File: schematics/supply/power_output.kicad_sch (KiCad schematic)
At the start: 41 parts, among them Q10 IRLML0030, Q6 STP13NK60Z, Q7 STP13NK60Z, U18 TL331, U19 INA169, U5 EL817, U9 IRS2153S

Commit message: Found and fixed issues in schematics.
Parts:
- R31, R32: value 5 -> 10
- R39: value 1K -> 680
- R39: value 70K -> 68K
- R39: value 30K -> 33K
- TR2: value ETD 49/25/16@N87 N19@1mm*2/7+7@1mm*4 -> ETD 49/25/16@N87 N18@1mm*2/7+7@1mm*4
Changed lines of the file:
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@@
     (stroke (width 0) (type default))
+  )
+  (text_box "Known issues:\n- Power Output generation will starts up when +5VSYS line is OFF"
+    (at 198.12 195.58 0) (size 82.55 76.2)
+    (stroke (width 0) (type default))
+    (fill (type none))
+    (effects (font (size 1.27 1.27)) (justify left top))
   )
   (text "100 KHz" (at 137.16 144.78 0)
@@
   (symbol (lib_id "Device:R") (at 176.53 114.3 90) (unit 1)
     (in_bom yes) (on_board yes) (dnp no) (fields_autoplaced)
-    (property "Reference" "R31" (at 176.53 109.22 90)
-      (effects (font (size 1.27 1.27)))
-    )
-    (property "Value" "5" (at 176.53 111.76 90)
+    (property "Reference" "R31" (at 176.53 107.95 90)
+      (effects (font (size 1.27 1.27)))
+    )
+    (property "Value" "10" (at 176.53 110.49 90)
       (effects (font (size 1.27 1.27)))
     )
@@
       (effects (font (size 1.27 1.27)))
     )
-    (property "Value" "1K" (at 337.82 95.25 0)
+    (property "Value" "680" (at 337.82 95.25 0)
       (effects (font (size 1.27 1.27)))
     )
@@
   (symbol (lib_id "Device:R") (at 176.53 146.05 90) (unit 1)
     (in_bom yes) (on_board yes) (dnp no) (fields_autoplaced)
-    (property "Reference" "R32" (at 176.53 140.97 90)
-      (effects (font (size 1.27 1.27)))
-    )
-    (property "Value" "5" (at 176.53 143.51 90)
+    (property "Reference" "R32" (at 176.53 139.7 90)
+      (effects (font (size 1.27 1.27)))
+    )
+    (property "Value" "10" (at 176.53 142.24 90)
       (effects (font (size 1.27 1.27)))
     )
@@
       (effects (font (size 1.27 1.27)))
     )
-    (property "Value" "70K" (at 292.1 91.44 90)
+    (property "Value" "68K" (at 292.1 91.44 90)
       (effects (font (size 1.27 1.27)))
     )
@@
       (effects (font (size 1.27 1.27)))
     )
-    (property "Value" "30K" (at 295.91 101.6 0)
+    (property "Value" "33K" (at 295.91 101.6 0)
       (effects (font (size 1.27 1.27)))
     )
@@
       (effects (font (size 1.27 1.27)))
     )
-    (property "Value" "ETD 49/25/16@N87 N19@1mm*2/7+7@1mm*4" (at 226.06 119.38 0)
-      (effects (font (size 1.27 1.27)))
-    )
+    (property "Value" "ETD 49/25/16@N87 N18@1mm*2/7+7@1mm*4" (at 226.06 119.38 0)
+      (effects (font (size 1.27 1.27)))
+    )

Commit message: Some changes
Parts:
- C17: value 100 nF -> 1 uF
- R53: value 49K5 -> 47K
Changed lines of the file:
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@@
       (effects (font (size 1.27 1.27)) (justify right))
     )
-    (property "Value" "49K5" (at 360.68 168.91 0)
+    (property "Value" "47K" (at 360.68 168.91 0)
       (effects (font (size 1.27 1.27)) (justify right))
     )
@@
       (effects (font (size 1.27 1.27)) (justify right))
     )
-    (property "Value" "100 nF" (at 121.92 114.3 0)
-      (effects (font (size 1.27 1.27)) (justify right))
-    )
+    (property "Value" "1 uF" (at 121.92 114.3 0)
+      (effects (font (size 1.27 1.27)) (justify right))
+    )

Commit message: Continue soldering and setting up hardware
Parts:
- D16: value SS16 -> STTH1R06A
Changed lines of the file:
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@@
   (symbol (lib_id "Device:D") (at 162.56 114.3 180) (unit 1)
     (in_bom yes) (on_board yes) (dnp no) (fields_autoplaced)
-    (property "Reference" "D16" (at 162.56 109.22 0)
+    (property "Reference" "D16" (at 162.56 107.95 0)
       (effects (font (size 1.27 1.27)))
     )
-    (property "Value" "SS16" (at 162.56 111.76 0)
+    (property "Value" "STTH1R06A" (at 162.56 110.49 0)
       (effects (font (size 1.27 1.27)))
     )

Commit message: supply board - power controllers changed; PWM logic changed
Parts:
- removed C17, C18, C21: 1 uF, Capacitor_SMD:C_0603_1608Metric, symbol Device:C
- removed C18: 22 uF, Capacitor_SMD:C_1210_3225Metric, symbol Device:C
- removed C19: 470 pF, Capacitor_SMD:C_0603_1608Metric, symbol Device:C
- removed D22: GNL-3012GD, Connector_JST:JST_XH_B2B-XH-A_1x02_P2.50mm_Vertical, symbol Device:LED
- removed Q10: IRLML0030, Package_TO_SOT_SMD:SOT-23, symbol Transistor_FET:IRLML0030
- removed Q6, Q7: STP13NK60Z, Package_TO_SOT_THT:TO-220-3_Vertical, symbol Device:Q_NMOS_GDS
- removed R25: 510, Resistor_SMD:R_0805_2012Metric, symbol Device:R
- removed R27: 10K, Resistor_SMD:R_0805_2012Metric, symbol Device:R
- removed R31, R32: 10, Resistor_SMD:R_0805_2012Metric, symbol Device:R
- removed R39: 680, Resistor_SMD:R_0805_2012Metric, symbol Device:R
- removed R39: 68K, Resistor_SMD:R_0805_2012Metric, symbol Device:R
- removed R39: 33K, Resistor_SMD:R_0805_2012Metric, symbol Device:R
- removed TP2: POWER_OUTPUT, TestPoint:TestPoint_Pad_D2.0mm, symbol Connector:TestPoint
- removed U18: TL331, Package_TO_SOT_SMD:SOT-23-5, symbol Comparator:TL331
- removed U5: EL817, Package_DIP:DIP-4_W7.62mm, symbol Isolator:EL817
- removed U9: IRS2153S, Package_SO:SOP-8_3.76x4.96mm_P1.27mm, symbol Driver_FET:IR2153
- added C10: 2 nF, Capacitor_SMD:C_0603_1608Metric, symbol Device:C
- added C16: 2200 uF@63V, Capacitor_THT:CP_Radial_D18.0mm_P7.50mm, symbol Device:C_Polarized
- added C4, C54: 1 uF, Capacitor_SMD:C_0603_1608Metric, symbol Device:C
- added C55, C67: 100 nF, Capacitor_SMD:C_0603_1608Metric, symbol Device:C
- added Q2, Q3: STP13NK60Z, Package_TO_SOT_THT:TO-220-3_Vertical, symbol Device:Q_NMOS_GDS
- added Q7 (x3): IRLML0030, Package_TO_SOT_SMD:SOT-23, symbol Transistor_FET:IRLML0030
- added R1 (x2): 220, Resistor_SMD:R_0805_2012Metric, symbol Device:R
- added R47: 22, Resistor_SMD:R_0805_2012Metric, symbol Device:R
- added R54, R56, R64, R68 (x2): 10K, Resistor_SMD:R_0805_2012Metric, symbol Device:R
- added R68: 1K, Resistor_SMD:R_0805_2012Metric, symbol Device:R
- added R9: 5K, Resistor_SMD:R_0805_2012Metric, symbol Device:R
- added U2 (x2): EL817, Package_DIP:DIP-4_W7.62mm, symbol Isolator:EL817
- added U23 (x2): IR2117, Package_SO:SOIC-8_3.9x4.9mm_P1.27mm, symbol My_Library:IR2117
- added U30: UC3525, Package_SO:SOIC-16W_7.5x10.3mm_P1.27mm, symbol Regulator_Controller:UC3525
- C14, C16: value CK45-B3DD331KYGNA -> К73-17 0.33 uF@630V; footprint Capacitor_THT:C_Disc_D7.5mm_W5.0mm_P5.00mm -> Capacitor_THT:C_Rect_L24.0mm_W12.2mm_P22.50mm_MKT
- R25: value 5K1@2W -> 100@2W
- renumbered R49 to R56, R50 to R57, R52 to R58, R53 to R59, U19 to U27
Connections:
- net +5V_VSYS: now also R1.2, R1.2
- net 400V: now also Q2.2 (D)
- net GND: now also C16.2, Q7.2 (S), Q7.2 (S), R68.1
- net GNDPWR: now also C10.2, C4.1, C55.2, C67.2, Q3.3 (S), Q7.2 (S), R56.2, R64.2, R68.2, R9.2, U23.3 (GND), U23.3 (GND), U23.6 (VS), U30.12 (GND)
- net POWER_OUTPUT_FB: now also Q7.1 (G)
- net RC_SNABBER_MIDDLEPOINT: now also C54.2, Q2.3 (S), Q3.2 (D), U23.6 (VS)
- net V_STANDBY: now also C4.2, U23.1 (VCC), U23.1 (VCC), U23.8 (VB), U30.13 (VC), U30.15 (VIN)
- net at D16.1 (K): now also C54.1, U23.8 (VB)
- net at D23.2 (K), L3.1: now also C16.1
- new net: R1.1, U2.1 (x2)
- new net: Q3.1 (G), U23.7 (OUT)
- new net: Q7.3 (D), U2.2 (x2)
- new net: Q7.1 (G), R68.1, U2.3
- new net: R9.1, U30.6 (RT)
- new net: U23.2 (IN), U30.11 (OUTA)
- new net: Q2.1 (G), U23.7 (OUT)
- new net: U23.2 (IN), U30.14 (OUTB)
- new net: C10.1, R47.1, U30.5 (CT)
- new net: R47.2, U30.7 (DISCH)
- new net: C55.1, U30.8 (SS)
- new net DCDC_2V5_VREF: R54.2, R56.1, U30.2 (NI)
- new net DCDC_5V_VREF: C67.1, R54.1, R68.1, U2.4, U2.4, U30.16 (REF)
- new net DCDC_FEEDBACK: R64.1, U2.3, U30.1 (INV)
- new net DCDC_SHUTDOWN: Q7.3 (D), R68.2, U30.10 (SD)
- new net PWR_SHUTDOWN#: Q7.1 (G), R68.2
- no-connect marks 0 -> 3
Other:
- note removed: "100 KHz"
- moved on the sheet: C14, C16, C18, C23, C24, CLR2, CLR3, CLR4, D23, L3, R25, R56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

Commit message: re-design supply board
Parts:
- added TP2: PW_B, TestPoint:TestPoint_Pad_1.0x1.0mm, symbol Connector:TestPoint
- added TP2: PW_A, TestPoint:TestPoint_Pad_1.0x1.0mm, symbol Connector:TestPoint
- renumbered R56 to R59, R57 to R60, R58 to R61, R59 to R62
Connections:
- net at U23.2 (IN), U30.11 (OUTA): now also TP2.1
- net at U23.2 (IN), U30.14 (OUTB): now also TP2.1

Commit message: Continue project
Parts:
- C51: renamed from C10; value 2 nF -> 2.2 nF
- C53: renamed from C4; value 1 uF -> 10 uF
- R50: renamed from R9; value 5K -> 2K2
- renumbered C67 to C50, C55 to C52, C23 to C55, C14 to C56, C24 to C57, C16 to C58, C16 to C59, C16 to C60, C18 to C61, C18 to C62, C18 to C63, D16 to D21, D23 to D22, L3 to L4, Q2 to Q10, Q3 to Q11, Q7 to Q8, Q7 to Q9, R54 to R48, R56 to R49, R68 to R51, R47 to R52, R1 to R53, R1 to R54, R64 to R55, R68 to R56, R68 to R57, R25 to R58, TP2 to TP17, TP2 to TP18, U2 to U22, U2 to U23, U30 to U24, U23 to U25, U23 to U26
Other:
- moved on the sheet: R50

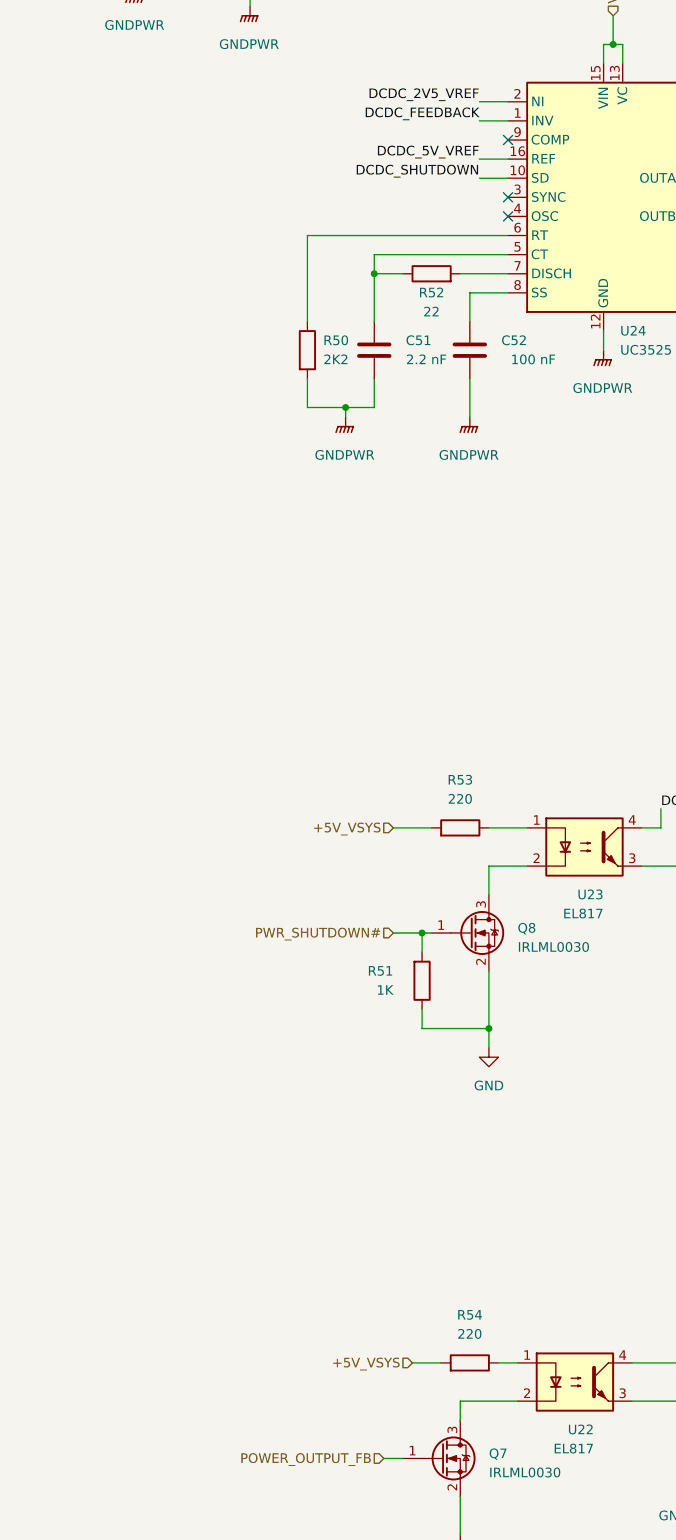
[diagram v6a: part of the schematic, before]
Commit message: some changes in schema. I found additional error. This commit saves changes before re-write some blocks
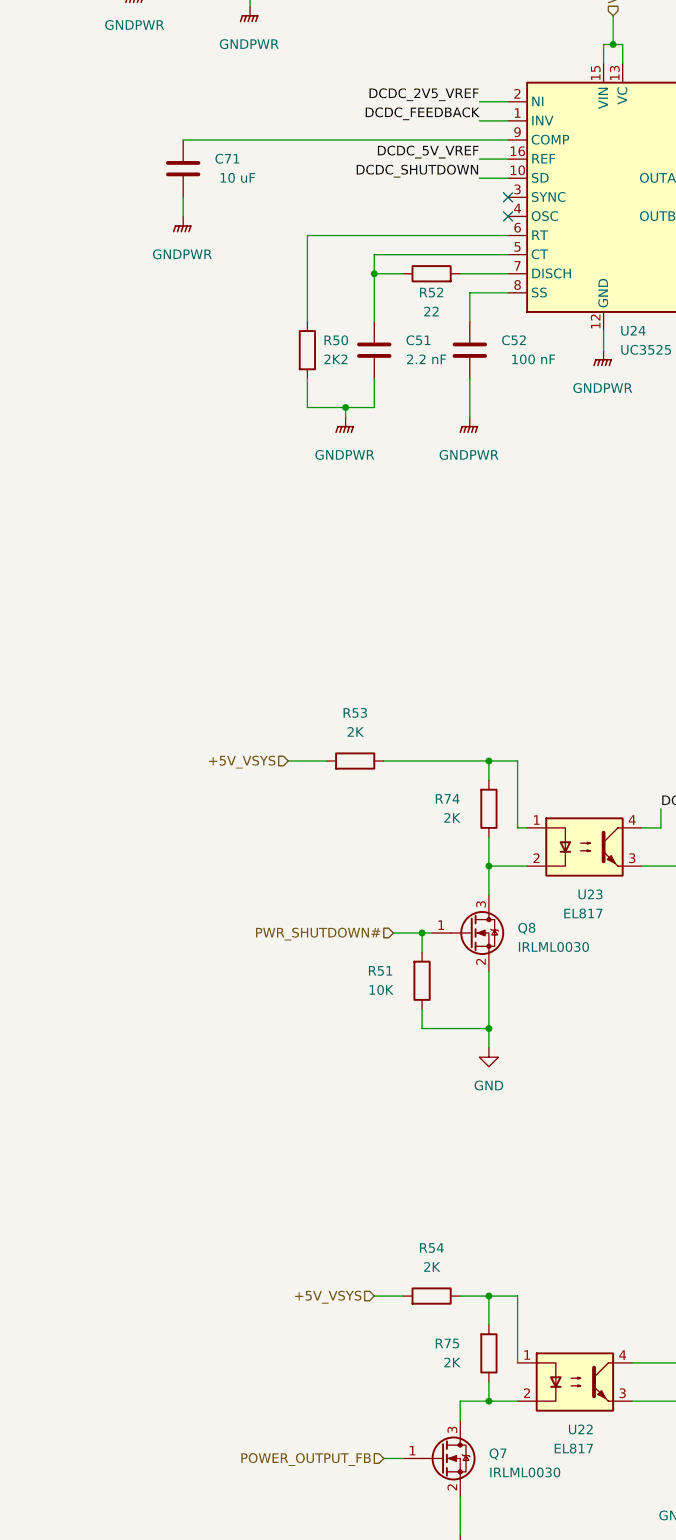
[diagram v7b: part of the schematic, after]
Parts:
- added C71: 10 uF, Capacitor_SMD:C_0603_1608Metric, symbol Device:C
- added R74, R75: 2K, Resistor_SMD:R_0805_2012Metric, symbol Device:R
- R51: value 1K -> 10K
- R53, R54: value 220 -> 2K
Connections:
- net GNDPWR: now also C71.2
- net at R54.1, U22.1: now also R75.2
- net at Q7.3 (D), U22.2: now also R75.1
- net at U24.9 (COMP): now also C71.1
- net at R53.1, U23.1: now also R74.2
- net at Q8.3 (D), U23.2: now also R74.1
- no-connect marks 3 -> 2
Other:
- moved on the sheet: R53, R54

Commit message: debugging DCDC converters... Standby supply works fine (noise level = 1,7%). At now Starting to debug PFC module
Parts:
- removed C54: 1 uF, Capacitor_SMD:C_0603_1608Metric, symbol Device:C
- removed C56, C58: К73-17 0.33 uF@630V, Capacitor_THT:C_Rect_L24.0mm_W12.2mm_P22.50mm_MKT, symbol Device:C
- removed D21: STTH1R06A, Diode_SMD:D_SMA, symbol Device:D
- removed R58: 100@2W, Resistor_THT:R_Axial_DIN0617_L17.0mm_D6.0mm_P5.08mm_Vertical, symbol Device:R
- removed TP17: PW_A, TestPoint:TestPoint_Pad_1.0x1.0mm, symbol Connector:TestPoint
- removed TP18: PW_B, TestPoint:TestPoint_Pad_1.0x1.0mm, symbol Connector:TestPoint
- removed U25, U26: IR2117, Package_SO:SOIC-8_3.9x4.9mm_P1.27mm, symbol My_Library:IR2117
- added C63: 47 uF@35V, Capacitor_THT:CP_Radial_D6.3mm_P2.50mm, symbol Device:C_Polarized
- added C67, C73: 100 nF, Capacitor_SMD:C_0603_1608Metric, symbol Device:C
- added C68: 1 uF, Capacitor_SMD:C_0603_1608Metric, symbol Device:C
- added C70: 47 uF@450V, Capacitor_THT:CP_Radial_D16.0mm_P7.50mm, symbol Device:C_Polarized
- added C72: К73-17 0.22 uF@630V, Capacitor_THT:C_Axial_L12.0mm_D6.5mm_P20.00mm_Horizontal, symbol Device:C
- added D23: STTH1R06A, Diode_SMD:D_SMA, symbol Device:D
- added R61, R62: 10, Resistor_SMD:R_0805_2012Metric, symbol Device:R
- added TP20: PV_H, TestPoint:TestPoint_Pad_1.0x1.0mm, symbol Connector:TestPoint
- added TP21: PV_L, TestPoint:TestPoint_Pad_1.0x1.0mm, symbol Connector:TestPoint
- added TP22: PV_GH, TestPoint:TestPoint_Pad_1.0x1.0mm, symbol Connector:TestPoint
- added TP23: PV_GL, TestPoint:TestPoint_Pad_1.0x1.0mm, symbol Connector:TestPoint
- added TP24: PV_MP, TestPoint:TestPoint_Pad_1.0x1.0mm, symbol Connector:TestPoint
- added U23: IRS21867S, Package_SO:SOIC-8_3.9x4.9mm_P1.27mm, symbol Driver_FET:IRS21867S
- renumbered C50 to C61, C71 to C62, C53 to C64, C51 to C65, C52 to C66, C55 to C69, C57 to C71, C59 to C74, C60 to C75, C61 to C76, C62 to C77, C63 to C78, D22 to D24, Q11 to Q10, Q7 to Q11, Q8 to Q7, Q9 to Q8, Q10 to Q9, R48 to R52, R49 to R53, R53 to R54, R50 to R55, R51 to R56, R52 to R57, R74 to R58, R56 to R59, R57 to R60, R54 to R63, R75 to R64, R55 to R65, R59 to R66, R60 to R67, R61 to R68, R62 to R69, U23 to U21, U24 to U22, U22 to U24, U27 to U25
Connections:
- net 400V: now also C70.1, C72.2
- net DCDC_FEEDBACK: now also C73.1
- net GNDPWR: now also C63.2, C67.2, C70.2, C72.1, C73.2, U23.4 (COM)
- net V_STANDBY: now also C63.1, C67.1, D23.2 (A), U23.1 (VCC)
- net at Q10.1 (G): now also R62.2, TP23.1
- net at U22.11 (OUTA): now also TP21.1, U23.3 (LIN)
- net at Q9.1 (G): now also R61.2, TP22.1
- net at U22.14 (OUTB): now also TP20.1, U23.2 (HIN)
- net RC_SNABBER_MIDDLEPOINT: no longer names the net of Q10.2 (D), Q9.3 (S), TR2.1, TR2.3
- net RC_SNABBER_MIDDLEPOINT: now also C68.2, TP24.1, U23.6 (VS)
- new net: R61.1, U23.7 (HO)
- new net: R62.1, U23.5 (LO)
- new net: C68.1, D23.1 (K), U23.8 (VB)
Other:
- moved on the sheet: C61, C62, C64, CLR2, CLR3, Q10, Q11, Q7, Q8, Q9, R52, R53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
